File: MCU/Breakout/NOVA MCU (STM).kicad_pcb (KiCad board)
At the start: 2 copper layers, 70 x 60 mm, 44 parts, among them J1101 Conn_01x06_Male, J501 Conn_01x12_Male, J502 Conn_01x12_Male, J503 Conn_01x12_Male, J504 Conn_01x12_Male, J601 USB_C_Receptacle, U301 STM32F401RBTx, U601 FT234XD-R, U701 MIC5219-3_3YM5-TR, Y401 ECS-260-8-36B-CKY-TR, Y402 JTX310

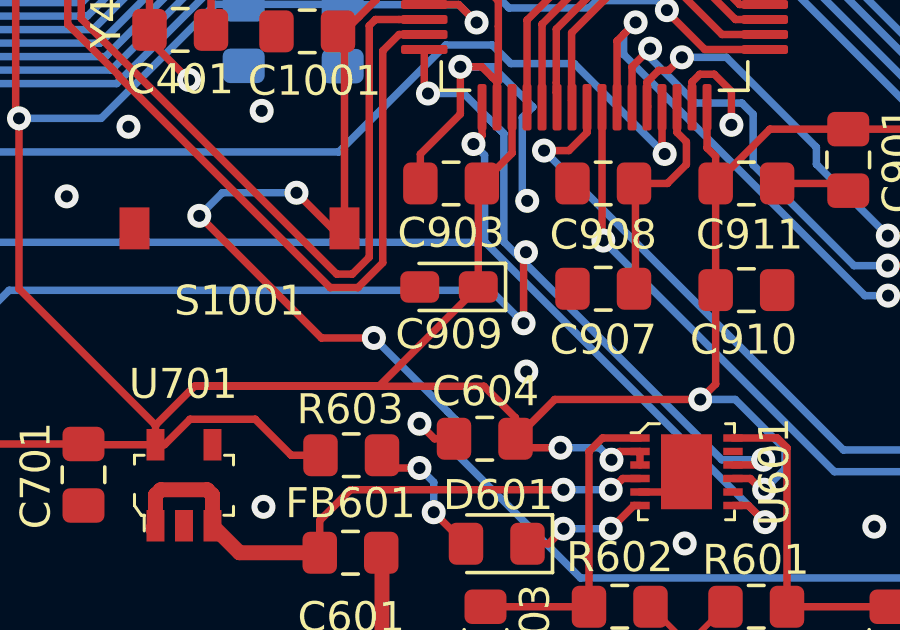
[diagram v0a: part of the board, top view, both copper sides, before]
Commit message: Found capacitor issue. Switched C909 to ceramic. Post-review
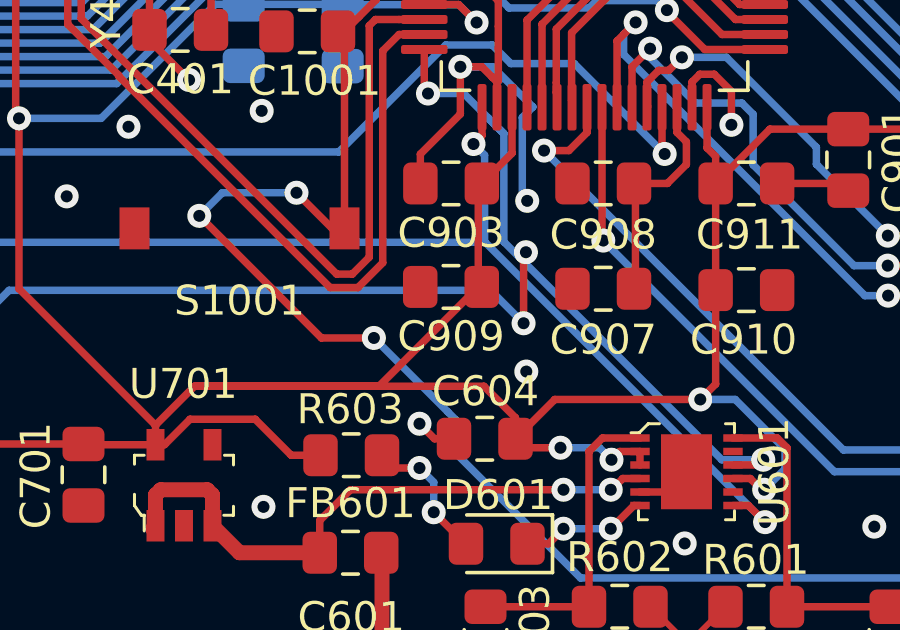
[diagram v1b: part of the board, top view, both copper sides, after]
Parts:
- C909: footprint NOVA MCU (STM):CP_EIA-2012-15_AVX-P_Pad1.30x1.05mm_HandSolder -> NOVA MCU (STM):C_0805_2012Metric_Pad1.15x1.40mm_HandSolder
- R401: value R_US -> TBD
- moved C909 0.07 mm to (126.0, 109.1)
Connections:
- net /STM32F401RBT6/REGULATOR /VUSB renamed VBUS
